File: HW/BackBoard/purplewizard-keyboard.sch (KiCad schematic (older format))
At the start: 47 parts, among them SW10 TACTILE, SW11 TACTILE, SW12 TACTILE, SW13 TACTILE, SW14 TACTILE, SW15 TACTILE, SW16 TACTILE, SW17 TACTILE, SW18 SKRHABE010, SW19 SKRHABE010, SW2 TACTILE, SW3 TACTILE, SW4 TACTILE, SW5 TACTILE, SW6 TACTILE, SW7 TACTILE, SW8 TACTILE, SW9 TACTILE, U7 ATtiny1617-M

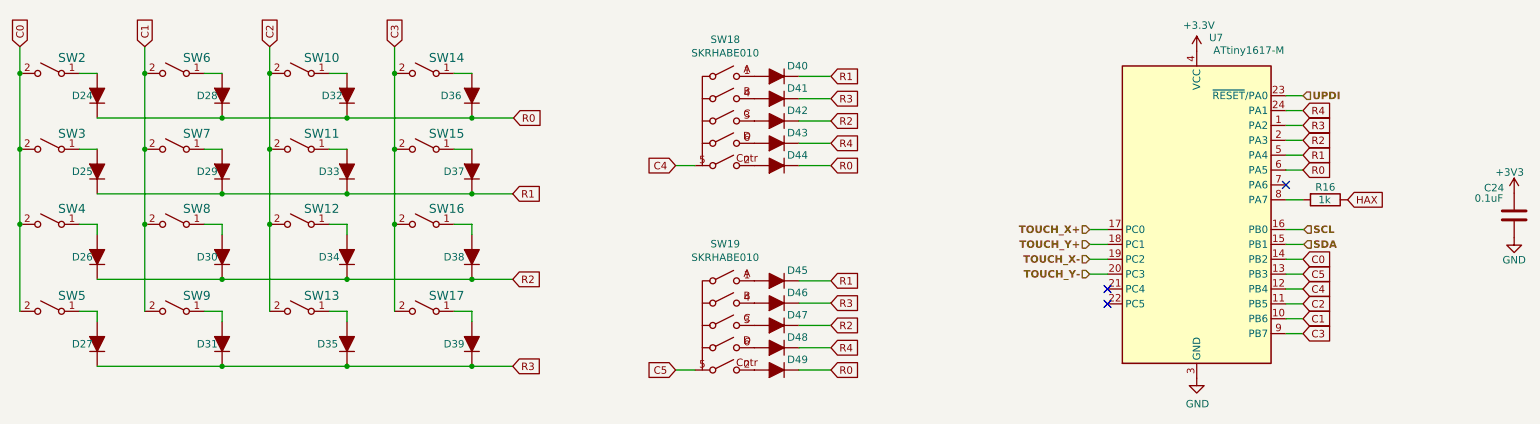
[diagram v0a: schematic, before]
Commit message: Backboard - Move LCD connector over .3mm for better fitment of ribbon - Fix audio chip missing exposed pad bond to ground - Remove nRESET signal from JTAG - Reuse freed pin above to run an interrupt line from the keyboard controller to the MCU to enable interrupt driven keyboard input.  Protos will have a hack-n-jump to be feature compatible - Enlarge mounting holes from 3mm to 3.2mm to allow for slightly sloppier fitments - Move traces and vias a little further away from top mounting holes as they are now being used for standoffs instead of just lanyard holes - Move vias from pads of ghosting diodes off to the side to prevent excess solder wicking - Modify UPDI programming pads to include vias for easier connection of programmer - Enlarged fiducials - Moved LCD CS from high to low - Added more breakout pads for the LCD on the back - Swapped to a PAM2305 voltage regulator - Hardwired the LCD LED to ground - Added some breakout for a couple of processor GPIO - Moved silk for speaker placement down a little - Added logo for PCBX Artboard - Remove mask over eyes
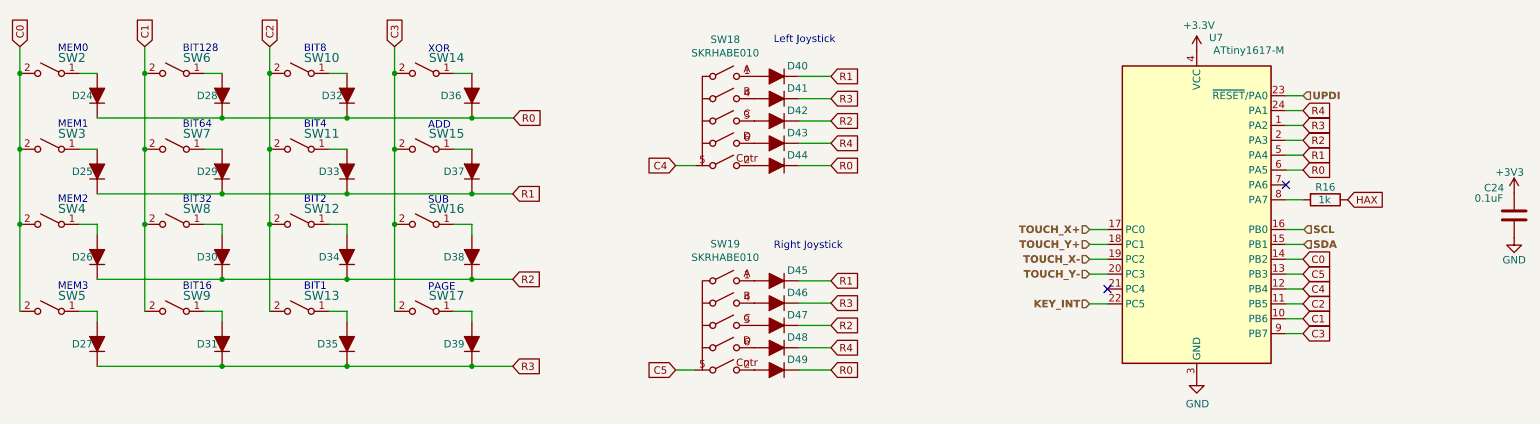
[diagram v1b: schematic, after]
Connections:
- net KEY_INT: now reaches U7.22 (PC5)
- no-connect marks 3 -> 2
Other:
- note added: "ADD"
- note added: "BIT1"
- note added: "BIT128"
- note added: "BIT16"
- note added: "BIT2"
- note added: "BIT32"
- note added: "BIT4"
- note added: "BIT64"
- note added: "BIT8"
- note added: "Left Joystick"
- note added: "MEM0"
- note added: "MEM1"
- note added: "MEM2"
- note added: "MEM3"
- note added: "PAGE"
- note added: "Right Joystick"
- note added: "SUB"
- note added: "XOR"
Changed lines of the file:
@@
 $EndComp
 NoConn ~ 9180 4390
-NoConn ~ 9180 4490
 NoConn ~ 10380 3690
 Wire Wire Line
@@
 	0    1    1    0
 $EndComp
+Text HLabel 9060 4490 0    50   Input ~ 10
+KEY_INT
+Wire Wire Line
+	9060 4490 9180 4490
+Text Notes 6935 2745 0    50   ~ 0
+Left Joystick
+Text Notes 6935 4130 0    50   ~ 0
+Right Joystick
+Text Notes 2120 2805 0    50   ~ 0
+MEM0
+Text Notes 2120 3315 0    50   ~ 0
+MEM1
+Text Notes 2120 3820 0    50   ~ 0
+MEM2
+Text Notes 2120 4405 0    50   ~ 0
+MEM3
+Text Notes 4610 2810 0    50   ~ 0
+XOR
+Text Notes 4610 3320 0    50   ~ 0
+ADD
+Text Notes 4610 3825 0    50   ~ 0
+SUB
+Text Notes 4610 4410 0    50   ~ 0
+PAGE
+Text Notes 2960 2805 0    50   ~ 0
+BIT128
+Text Notes 2960 3315 0    50   ~ 0
+BIT64
+Text Notes 2960 3820 0    50   ~ 0
+BIT32
+Text Notes 2960 4405 0    50   ~ 0
+BIT16
+Text Notes 3775 2805 0    50   ~ 0
+BIT8
+Text Notes 3775 3315 0    50   ~ 0
+BIT4
+Text Notes 3775 3820 0    50   ~ 0
+BIT2
+Text Notes 3775 4405 0    50   ~ 0
+BIT1
 $EndSCHEMATC
